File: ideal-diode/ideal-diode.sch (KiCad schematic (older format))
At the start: 5 parts, among them J1 Conn_01x03, Q1 BC857BS, Q2 IRLML2244

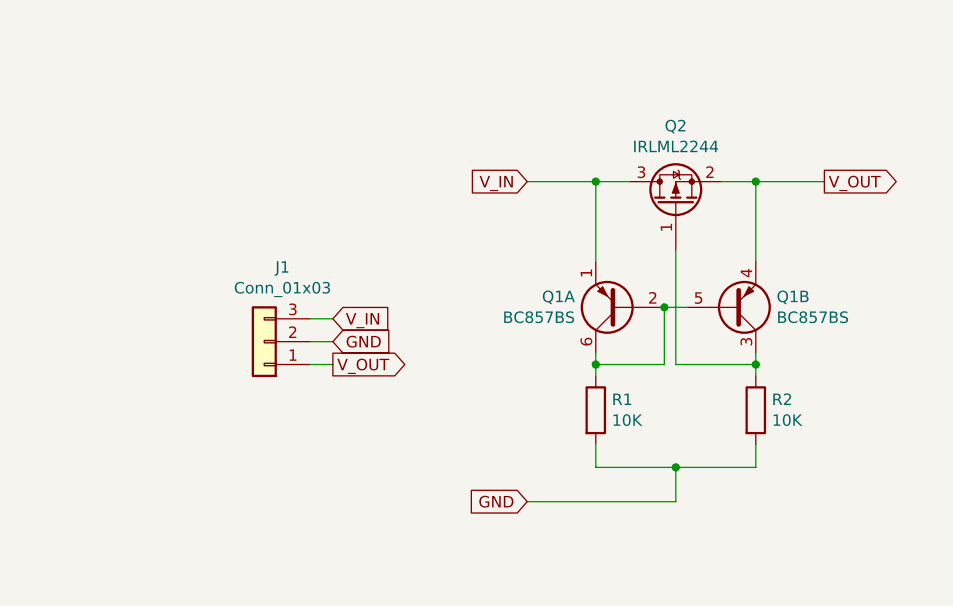
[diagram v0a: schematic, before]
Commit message: ideal-diod: add figures
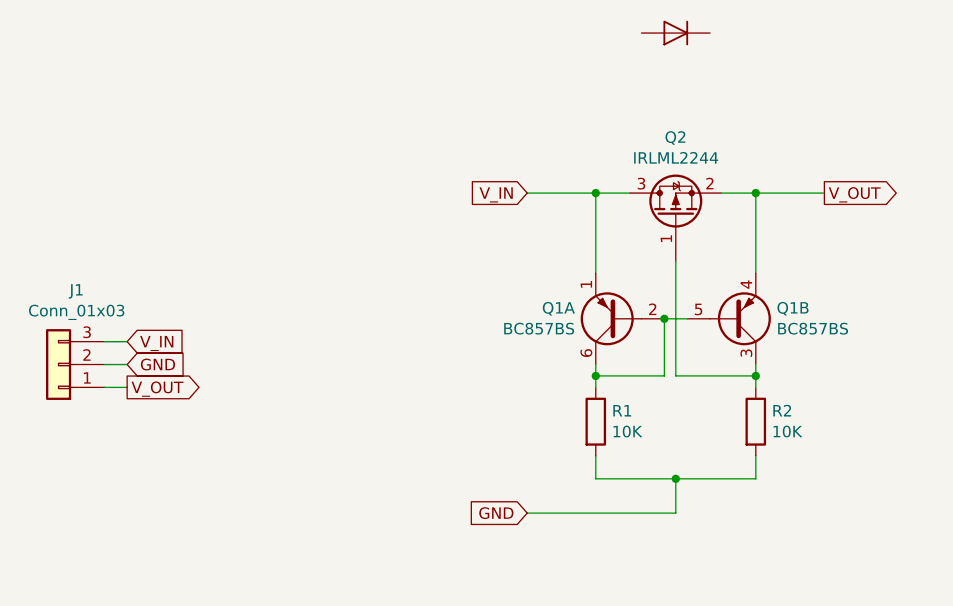
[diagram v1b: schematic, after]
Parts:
- added D1: D, symbol Device:D
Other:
- moved on the sheet: J1, Q1A, Q1B, Q2, R1, R2
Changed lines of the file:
@@
 EESchema Schematic File Version 4
+LIBS:ideal-diode-cache
 EELAYER 26 0
 EELAYER END
@@
 L Transistor_BJT:BC857BS Q1
 U 1 1 5D151D2B
-P 4300 2350
-F 0 "Q1" H 4491 2304 50  0000 L CNN
-F 1 "BC857BS" H 4491 2395 50  0000 L CNN
-F 2 "Package_TO_SOT_SMD:SOT-363_SC-70-6" H 4500 2450 50  0001 C CNN
-F 3 "http://www.nxp.com/documents/data_sheet/BC857BS.pdf" H 4300 2350 50  0001 C CNN
-	1    4300 2350
+P 4300 2400
+F 0 "Q1" H 4491 2354 50  0000 L CNN
+F 1 "BC857BS" H 4491 2445 50  0000 L CNN
+F 2 "Package_TO_SOT_SMD:SOT-363_SC-70-6" H 4500 2500 50  0001 C CNN
+F 3 "http://www.nxp.com/documents/data_sheet/BC857BS.pdf" H 4300 2400 50  0001 C CNN
+	1    4300 2400
 	-1   0    0    1
 $EndComp
@@
 L Transistor_BJT:BC857BS Q1
 U 2 1 5D151D7E
-P 4800 2350
-F 0 "Q1" H 4991 2304 50  0000 L CNN
-F 1 "BC857BS" H 4991 2395 50  0000 L CNN
-F 2 "Package_TO_SOT_SMD:SOT-363_SC-70-6" H 5000 2450 50  0001 C CNN
-F 3 "http://www.nxp.com/documents/data_sheet/BC857BS.pdf" H 4800 2350 50  0001 C CNN
-	2    4800 2350
+P 4800 2400
+F 0 "Q1" H 4991 2354 50  0000 L CNN
+F 1 "BC857BS" H 4991 2445 50  0000 L CNN
+F 2 "Package_TO_SOT_SMD:SOT-363_SC-70-6" H 5000 2500 50  0001 C CNN
+F 3 "http://www.nxp.com/documents/data_sheet/BC857BS.pdf" H 4800 2400 50  0001 C CNN
+	2    4800 2400
 	1    0    0    1
 $EndComp
@@
 L Device:Q_PMOS_GSD Q2
 U 1 1 5D151FEF
-P 4550 1900
-F 0 "Q2" V 4893 1900 50  0000 C CNN
-F 1 "IRLML2244" V 4802 1900 50  0000 C CNN
-F 2 "" H 4750 2000 50  0001 C CNN
-F 3 "~" H 4550 1900 50  0001 C CNN
-	1    4550 1900
+P 4550 1950
+F 0 "Q2" V 4893 1950 50  0000 C CNN
+F 1 "IRLML2244" V 4802 1950 50  0000 C CNN
+F 2 "" H 4750 2050 50  0001 C CNN
+F 3 "~" H 4550 1950 50  0001 C CNN
+	1    4550 1950
 	0    -1   -1   0
 $EndComp
@@
 L Device:R R1
 U 1 1 5D152127
-P 4200 2800
-F 0 "R1" H 4270 2846 50  0000 L CNN
-F 1 "10K" H 4270 2755 50  0000 L CNN
-F 2 "" V 4130 2800 50  0001 C CNN
-F 3 "~" H 4200 2800 50  0001 C CNN
-	1    4200 2800
+P 4200 2850
+F 0 "R1" H 4270 2896 50  0000 L CNN
+F 1 "10K" H 4270 2805 50  0000 L CNN
+F 2 "" V 4130 2850 50  0001 C CNN
+F 3 "~" H 4200 2850 50  0001 C CNN
+	1    4200 2850
 	1    0    0    -1
 $EndComp
@@
 L Device:R R2
 U 1 1 5D152191
-P 4900 2800
-F 0 "R2" H 4970 2846 50  0000 L CNN
-F 1 "10K" H 4970 2755 50  0000 L CNN
-F 2 "" V 4830 2800 50  0001 C CNN
-F 3 "~" H 4900 2800 50  0001 C CNN
-	1    4900 2800
+P 4900 2850
+F 0 "R2" H 4970 2896 50  0000 L CNN
+F 1 "10K" H 4970 2805 50  0000 L CNN
+F 2 "" V 4830 2850 50  0001 C CNN
+F 3 "~" H 4900 2850 50  0001 C CNN
+	1    4900 2850
 	1    0    0    -1
 $EndComp
 Wire Wire Line
-	4200 2650 4200 2600
+	4200 2700 4200 2650
 Wire Wire Line
-	4500 2350 4600 2350
+	4500 2400 4600 2400
+Wire Wire Line
+	4900 2700 4900 2650
+Wire Wire Line
+	4200 2200 4200 1850
+Wire Wire Line
+	4200 1850 4350 1850
+Wire Wire Line
+	4750 1850 4900 1850
+Wire Wire Line
+	4900 1850 4900 2200
+Wire Wire Line
+	4550 2150 4550 2650
+Wire Wire Line
+	4550 2650 4900 2650
+Connection ~ 4900 2650
 Wire Wire Line
 	4900 2650 4900 2600
 Wire Wire Line
-	4200 2150 4200 1800
+	4500 2400 4500 2650
 Wire Wire Line
-	4200 1800 4350 1800
+	4500 2650 4200 2650
+Connection ~ 4500 2400
+Connection ~ 4200 2650
 Wire Wire Line
-	4750 1800 4900 1800
+	4200 2650 4200 2600
 Wire Wire Line
-	4900 1800 4900 2150
+	4200 3000 4200 3100
 Wire Wire Line
-	4550 2100 4550 2600
+	4200 3100 4550 3100
 Wire Wire Line
-	4550 2600 4900 2600
-Connection ~ 4900 2600
-Wire Wire Line
-	4900 2600 4900 2550
-Wire Wire Line
-	4500 2350 4500 2600
-Wire Wire Line
-	4500 2600 4200 2600
-Connection ~ 4500 2350
-Connection ~ 4200 2600
-Wire Wire Line
-	4200 2600 4200 2550
-Wire Wire Line
-	4200 2950 4200 3050
-Wire Wire Line
-	4200 3050 4550 3050
-Wire Wire Line
-	4900 3050 4900 2950
+	4900 3100 4900 3000
 $Comp
 L Connector_Generic:Conn_01x03 J1
 U 1 1 5D15287F
-P 2750 2500
-F 0 "J1" H 2670 2175 50  0000 C CNN
-F 1 "Conn_01x03" H 2670 2266 50  0000 C CNN
-F 2 "" H 2750 2500 50  0001 C CNN
-F 3 "~" H 2750 2500 50  0001 C CNN
-	1    2750 2500
+P 1850 2600
+F 0 "J1" H 1770 2275 50  0000 C CNN
+F 1 "Conn_01x03" H 1770 2366 50  0000 C CNN
+F 2 "" H 1850 2600 50  0001 C CNN
+F 3 "~" H 1850 2600 50  0001 C CNN
+	1    1850 2600
 	-1   0    0    1
 $EndComp
-Text GLabel 3900 1800 0    50   Input ~ 0
+Text GLabel 3900 1850 0    50   Input ~ 0
 V_IN
-Text GLabel 5200 1800 2    50   Output ~ 0
+Text GLabel 5200 1850 2    50   Output ~ 0
 V_OUT
-Text GLabel 3900 3200 0    50   Input ~ 0
+Text GLabel 3900 3250 0    50   Input ~ 0
 GND
 Wire Wire Line
-	4900 1800 5200 1800
-Connection ~ 4900 1800
+	4900 1850 5200 1850
+Connection ~ 4900 1850
 Wire Wire Line
-	3900 1800 4200 1800
-Connection ~ 4200 1800
+	3900 1850 4200 1850
+Connection ~ 4200 1850
 Wire Wire Line
-	3900 3200 4550 3200
+	3900 3250 4550 3250
 Wire Wire Line
-	4550 3200 4550 3050
-Connection ~ 4550 3050
+	4550 3250 4550 3100
+Connection ~ 4550 3100
 Wire Wire Line
-	4550 3050 4900 3050
-Text GLabel 3050 2400 2    50   Input ~ 0
+	4550 3100 4900 3100
+Text GLabel 2150 2500 2    50   Input ~ 0
 V_IN
-Text GLabel 3050 2600 2    50   Output ~ 0
+Text GLabel 2150 2700 2    50   Output ~ 0
 V_OUT
-Text GLabel 3050 2500 2    50   Input ~ 0
+Text GLabel 2150 2600 2    50   Input ~ 0
 GND
 Wire Wire Line
-	2950 2400 3050 2400
+	2050 2500 2150 2500
 Wire Wire Line
-	2950 2500 3050 2500
+	2050 2600 2150 2600
 Wire Wire Line
-	2950 2600 3050 2600
+	2050 2700 2150 2700
+$Comp
+L Device:D D1
+U 1 1 5D17E3EA
+P 4550 1150
+F 0 "D1" H 4550 1026 50  0001 C CNN
+F 1 "D" H 4550 1025 50  0001 C CNN
+F 2 "" H 4550 1150 50  0001 C CNN
+F 3 "~" H 4550 1150 50  0001 C CNN
+	1    4550 1150
+	-1   0    0    1
+$EndComp
 $EndSCHEMATC

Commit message: Updated ideal-diode
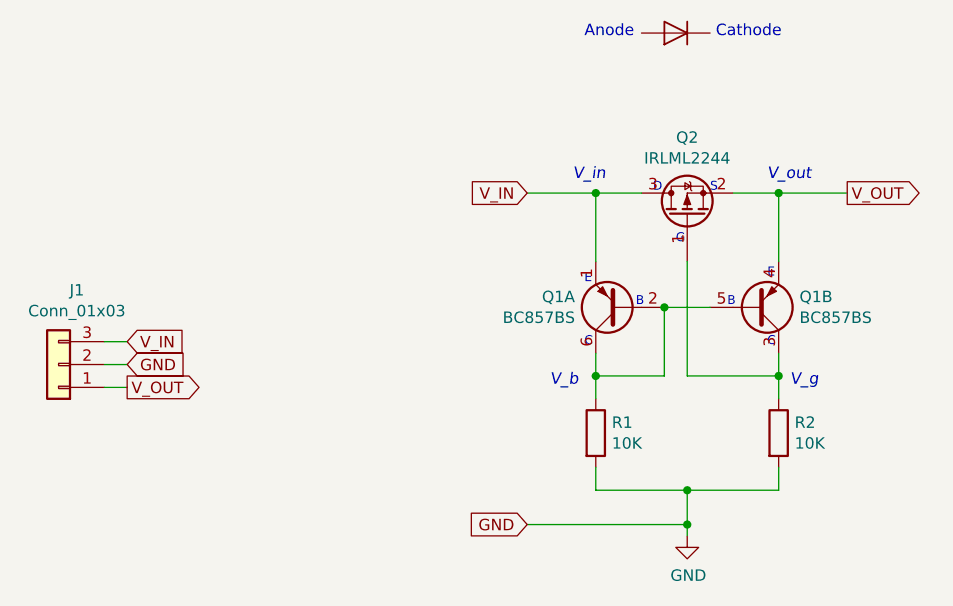
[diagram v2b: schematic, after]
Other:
- note added: "Anode"
- note added: "B"
- note added: "C"
- note added: "Cathode"
- note added: "D"
- note added: "E"
- note added: "G"
- note added: "S"
- note added: "V_b"
- note added: "V_g"
- note added: "V_in"
- note added: "V_out"
- moved on the sheet: Q1A, Q1B, Q2, R1, R2
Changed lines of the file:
@@
 L Transistor_BJT:BC857BS Q1
 U 1 1 5D151D2B
-P 4300 2400
-F 0 "Q1" H 4491 2354 50  0000 L CNN
-F 1 "BC857BS" H 4491 2445 50  0000 L CNN
-F 2 "Package_TO_SOT_SMD:SOT-363_SC-70-6" H 4500 2500 50  0001 C CNN
-F 3 "http://www.nxp.com/documents/data_sheet/BC857BS.pdf" H 4300 2400 50  0001 C CNN
-	1    4300 2400
+P 4300 2350
+F 0 "Q1" H 4491 2304 50  0000 L CNN
+F 1 "BC857BS" H 4491 2395 50  0000 L CNN
+F 2 "Package_TO_SOT_SMD:SOT-363_SC-70-6" H 4500 2450 50  0001 C CNN
+F 3 "http://www.nxp.com/documents/data_sheet/BC857BS.pdf" H 4300 2350 50  0001 C CNN
+	1    4300 2350
 	-1   0    0    1
 $EndComp
@@
 L Transistor_BJT:BC857BS Q1
 U 2 1 5D151D7E
-P 4800 2400
-F 0 "Q1" H 4991 2354 50  0000 L CNN
-F 1 "BC857BS" H 4991 2445 50  0000 L CNN
-F 2 "Package_TO_SOT_SMD:SOT-363_SC-70-6" H 5000 2500 50  0001 C CNN
-F 3 "http://www.nxp.com/documents/data_sheet/BC857BS.pdf" H 4800 2400 50  0001 C CNN
-	2    4800 2400
+P 4900 2350
+F 0 "Q1" H 5091 2304 50  0000 L CNN
+F 1 "BC857BS" H 5091 2395 50  0000 L CNN
+F 2 "Package_TO_SOT_SMD:SOT-363_SC-70-6" H 5100 2450 50  0001 C CNN
+F 3 "http://www.nxp.com/documents/data_sheet/BC857BS.pdf" H 4900 2350 50  0001 C CNN
+	2    4900 2350
 	1    0    0    1
 $EndComp
@@
 L Device:Q_PMOS_GSD Q2
 U 1 1 5D151FEF
-P 4550 1950
-F 0 "Q2" V 4893 1950 50  0000 C CNN
-F 1 "IRLML2244" V 4802 1950 50  0000 C CNN
-F 2 "" H 4750 2050 50  0001 C CNN
-F 3 "~" H 4550 1950 50  0001 C CNN
-	1    4550 1950
+P 4600 1950
+F 0 "Q2" V 4943 1950 50  0000 C CNN
+F 1 "IRLML2244" V 4852 1950 50  0000 C CNN
+F 2 "" H 4800 2050 50  0001 C CNN
+F 3 "~" H 4600 1950 50  0001 C CNN
+	1    4600 1950
 	0    -1   -1   0
 $EndComp
@@
 L Device:R R1
 U 1 1 5D152127
-P 4200 2850
-F 0 "R1" H 4270 2896 50  0000 L CNN
-F 1 "10K" H 4270 2805 50  0000 L CNN
-F 2 "" V 4130 2850 50  0001 C CNN
-F 3 "~" H 4200 2850 50  0001 C CNN
-	1    4200 2850
+P 4200 2900
+F 0 "R1" H 4270 2946 50  0000 L CNN
+F 1 "10K" H 4270 2855 50  0000 L CNN
+F 2 "" V 4130 2900 50  0001 C CNN
+F 3 "~" H 4200 2900 50  0001 C CNN
+	1    4200 2900
 	1    0    0    -1
 $EndComp
@@
 L Device:R R2
 U 1 1 5D152191
-P 4900 2850
-F 0 "R2" H 4970 2896 50  0000 L CNN
-F 1 "10K" H 4970 2805 50  0000 L CNN
-F 2 "" V 4830 2850 50  0001 C CNN
-F 3 "~" H 4900 2850 50  0001 C CNN
-	1    4900 2850
+P 5000 2900
+F 0 "R2" H 5070 2946 50  0000 L CNN
+F 1 "10K" H 5070 2855 50  0000 L CNN
+F 2 "" V 4930 2900 50  0001 C CNN
+F 3 "~" H 5000 2900 50  0001 C CNN
+	1    5000 2900
 	1    0    0    -1
 $EndComp
 Wire Wire Line
-	4200 2700 4200 2650
+	4200 2750 4200 2650
 Wire Wire Line
-	4500 2400 4600 2400
+	4500 2350 4700 2350
 Wire Wire Line
-	4900 2700 4900 2650
+	5000 2750 5000 2650
 Wire Wire Line
-	4200 2200 4200 1850
+	4200 2150 4200 1850
 Wire Wire Line
-	4200 1850 4350 1850
+	4200 1850 4400 1850
 Wire Wire Line
-	4750 1850 4900 1850
+	4800 1850 5000 1850
 Wire Wire Line
-	4900 1850 4900 2200
+	5000 1850 5000 2150
 Wire Wire Line
-	4550 2150 4550 2650
+	4600 2150 4600 2650
 Wire Wire Line
-	4550 2650 4900 2650
-Connection ~ 4900 2650
+	4600 2650 5000 2650
+Connection ~ 5000 2650
 Wire Wire Line
-	4900 2650 4900 2600
-Wire Wire Line
-	4500 2400 4500 2650
+	5000 2650 5000 2550
 Wire Wire Line
 	4500 2650 4200 2650
-Connection ~ 4500 2400
 Connection ~ 4200 2650
 Wire Wire Line
-	4200 2650 4200 2600
+	4200 2650 4200 2550
 Wire Wire Line
-	4200 3000 4200 3100
+	4200 3050 4200 3150
 Wire Wire Line
-	4200 3100 4550 3100
+	4200 3150 4600 3150
 Wire Wire Line
-	4900 3100 4900 3000
+	5000 3150 5000 3050
 $Comp
 L Connector_Generic:Conn_01x03 J1
@@
 Text GLabel 3900 1850 0    50   Input ~ 0
 V_IN
-Text GLabel 5200 1850 2    50   Output ~ 0
+Text GLabel 5300 1850 2    50   Output ~ 0
 V_OUT
-Text GLabel 3900 3250 0    50   Input ~ 0
+Text GLabel 3900 3300 0    50   Input ~ 0
 GND
 Wire Wire Line
-	4900 1850 5200 1850
-Connection ~ 4900 1850
+	5000 1850 5300 1850
+Connection ~ 5000 1850
 Wire Wire Line
 	3900 1850 4200 1850
 Connection ~ 4200 1850
 Wire Wire Line
-	3900 3250 4550 3250
+	3900 3300 4600 3300
 Wire Wire Line
-	4550 3250 4550 3100
-Connection ~ 4550 3100
+	4600 3300 4600 3150
+Connection ~ 4600 3150
 Wire Wire Line
-	4550 3100 4900 3100
+	4600 3150 5000 3150
 Text GLabel 2150 2500 2    50   Input ~ 0
 V_IN
@@
 	-1   0    0    1
 $EndComp
+Connection ~ 4500 2350
+Wire Wire Line
+	4500 2350 4500 2650
+Text Notes 4100 1800 0    50   Italic 0
+V_in
+Text Notes 4950 1800 0    50   Italic 0
+V_out
+Text Notes 4000 2700 0    50   Italic 0
+V_b
+$Comp
+L power:GND #PWR?
+U 1 1 5D18A703
+P 4600 3350
+F 0 "#PWR?" H 4600 3100 50  0001 C CNN
+F 1 "GND" H 4605 3177 50  0000 C CNN
+F 2 "" H 4600 3350 50  0001 C CNN
+F 3 "" H 4600 3350 50  0001 C CNN
+	1    4600 3350
+	1    0    0    -1
+$EndComp
+Wire Wire Line
+	4600 3350 4600 3300
+Connection ~ 4600 3300
+Text Notes 5050 2700 0    50   Italic 0
+V_g
+Text Notes 4150 1175 0    50   ~ 0
+Anode
+Text Notes 4725 1175 0    50   ~ 0
+Cathode
+Text Notes 4550 2075 0    39   ~ 0
+G
+Text Notes 4700 1850 0    39   ~ 0
+S
+Text Notes 4450 1850 0    39   ~ 0
+D
+Text Notes 4150 2250 0    39   ~ 0
+E
+Text Notes 4150 2525 0    39   ~ 0
+C
+Text Notes 4375 2350 0    39   ~ 0
+B
+Text Notes 4950 2225 0    39   ~ 0
+E
+Text Notes 4950 2525 0    39   ~ 0
+C
+Text Notes 4775 2350 0    39   ~ 0
+B
 $EndSCHEMATC
